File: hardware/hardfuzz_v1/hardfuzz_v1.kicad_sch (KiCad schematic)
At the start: 0 parts

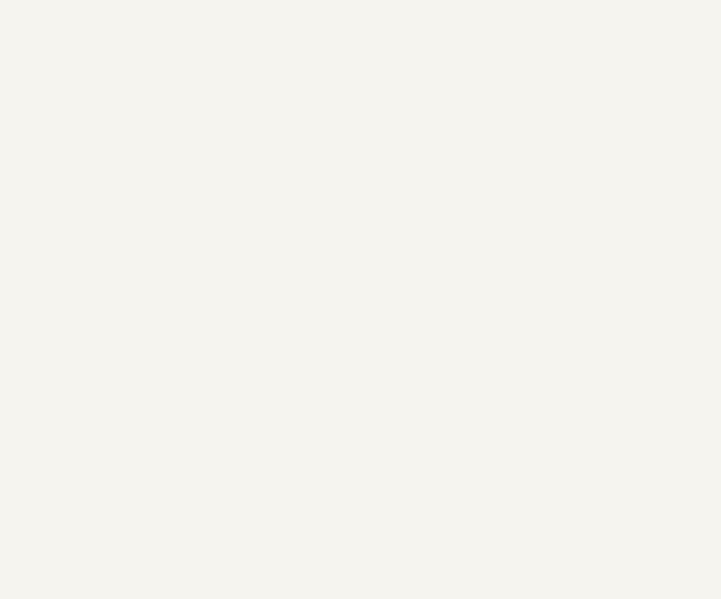
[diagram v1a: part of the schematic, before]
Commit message: v2: standalone/BLE architecture doc + ESP32 controller added to the board
docs/HardFuzz_v2_Standalone.md: computer-free architecture — an on-board ESP32-S3
runs the header-only C++ campaign engine (ports nearly as-is), arms the FPGA over
UART, drives the DUT, and streams results to a phone app over BLE. Includes the GATT
service definition and the host-engine -> ESP32 mapping.

Design: gen/esp32_sheet.py adds the ESP32-S3-WROOM-1 (power, EN/IO0 boot circuits,
UART to FPGA via the freed FT2232 ch-B control nets, UART to a DUT header, USB-C for
programming, BLE LED). Regenerated schematic (7 sheets, 83 parts) + PCB (loads,
ESP32 placed). FT2232 keeps JTAG; ESP32 owns the runtime control path.

Co-Authored-By: Claude Opus 4.8 <noreply@anthropic.com>
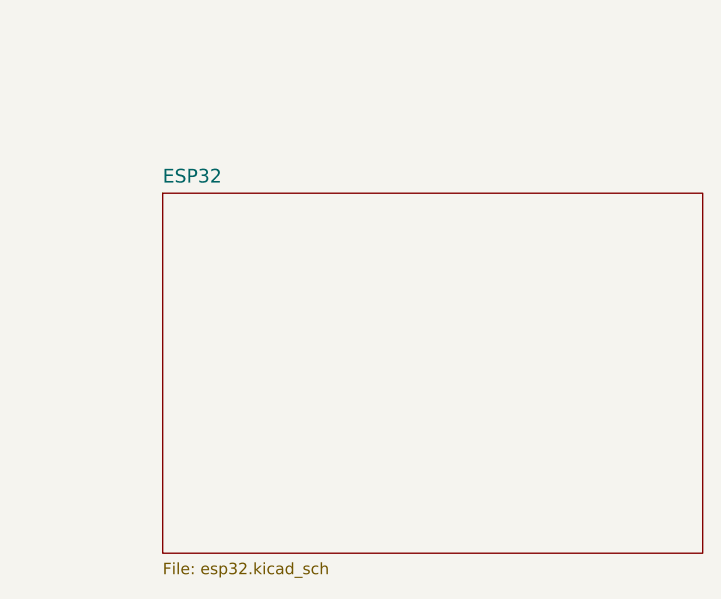
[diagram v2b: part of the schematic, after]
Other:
- added sheet ESP32 (esp32.kicad_sch)
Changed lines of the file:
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@@
 		(instances
 			(project "hardfuzz_v1"
-				(path "/287a9ed2-a26a-4469-8d2c-da808579c5eb" (page "2"))))
+				(path "/e670de3b-3b13-4b40-b5e5-d70ed10bfe5a" (page "2"))))
 	)
 	(sheet
@@
 		(instances
 			(project "hardfuzz_v1"
-				(path "/287a9ed2-a26a-4469-8d2c-da808579c5eb" (page "3"))))
+				(path "/e670de3b-3b13-4b40-b5e5-d70ed10bfe5a" (page "3"))))
 	)
 	(sheet
@@
 		(instances
 			(project "hardfuzz_v1"
-				(path "/287a9ed2-a26a-4469-8d2c-da808579c5eb" (page "4"))))
+				(path "/e670de3b-3b13-4b40-b5e5-d70ed10bfe5a" (page "4"))))
 	)
 	(sheet
@@
 		(instances
 			(project "hardfuzz_v1"
-				(path "/287a9ed2-a26a-4469-8d2c-da808579c5eb" (page "5"))))
+				(path "/e670de3b-3b13-4b40-b5e5-d70ed10bfe5a" (page "5"))))
 	)
 	(sheet
@@
 		(instances
 			(project "hardfuzz_v1"
-				(path "/287a9ed2-a26a-4469-8d2c-da808579c5eb" (page "6"))))
+				(path "/e670de3b-3b13-4b40-b5e5-d70ed10bfe5a" (page "6"))))
+	)
+	(sheet
+		(at 210 100)
+		(size 60 40)
+		(exclude_from_sim no)
+		(in_bom yes)
+		(on_board yes)
+		(dnp no)
+		(fields_autoplaced yes)
+		(stroke (width 0.1524) (type solid))
+		(fill (color 0 0 0 0.0000))
+		(property "Sheetname" "ESP32" (at 210 99 0)
+			(effects (font (size 1.524 1.524)) (justify left bottom)))
+		(property "Sheetfile" "esp32.kicad_sch" (at 210 141 0)
+			(effects (font (size 1.27 1.27)) (justify left top)))
+		(instances
+			(project "hardfuzz_v1"
+				(path "/e670de3b-3b13-4b40-b5e5-d70ed10bfe5a" (page "7"))))
 	)
 	(sheet_instances
